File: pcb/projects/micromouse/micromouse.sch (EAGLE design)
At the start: 52 parts, among them M1 332-06, M2 332-06, U1 DSPIC33FJ64MC804-H/PTTQFP44_1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, U2 UA78M33CKCS, U3 UA78M05CKCS

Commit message: Replace some pin connectors
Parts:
- removed DIST1+, DIST1-, DIST1S, DIST2+, DIST2-, DIST2S, DIST3+, DIST3-, DIST3S, PAD+, PAD-: (no value), wirepad:SMD2
- removed M1, M2: 332-06, con-garry:332-06
- added DIST1, DIST2, DIST3: (no value), con-lstb:MA03-1
- added G1: AB9V, battery:AB9V
- added MOTOR1, MOTOR2: (no value), con-lstb:MA03-2
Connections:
- net +5V: now also DIST1.3, DIST2.3, DIST3.3; no longer DIST1+.P, DIST2+.P, DIST3+.P
- net DSENS1: now also DIST1.2; no longer DIST1S.P
- net DSENS2: now also DIST2.2; no longer DIST2S.P
- net DSENS3: now also DIST3.2; no longer DIST3S.P
- net GND: now also DIST1.1, DIST2.1, DIST3.1, G1.-, MOTOR1.3, MOTOR2.3; no longer DIST1-.P, DIST2-.P, DIST3-.P, M1-3.S, M2-3.S, PAD-.P
- net M1+: now also D2.C, D4.A, MOTOR1.2; no longer D3.C, D5.A, M1-6.S
- net M1-: now also D3.C, D5.A, MOTOR1.1; no longer D2.C, D4.A, M1-5.S
- net M1_EA: now also MOTOR1.6; no longer M1-2.S
- net M1_EB: now also MOTOR1.5; no longer M1-1.S
- net M2+: now also MOTOR2.2; no longer M2-6.S
- net M2-: now also MOTOR2.1; no longer M2-5.S
- net M2_EA: now also MOTOR2.6; no longer M2-2.S
- net M2_EB: now also MOTOR2.5; no longer M2-1.S
- net PAD+: now also G1.+; no longer PAD+.P
- net VDD: now also MOTOR1.4, MOTOR2.4; no longer M1-4.S, M2-4.S
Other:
- note added: "TODO: - Double-check pin connections for programmer and UART connector - Check connection for buttons"
- note removed: "TODO: - Decoupling capacitor for sensors? - Package for: - Diodes - Crystal - Buttons - Voltage Regulators"
- moved on the sheet: D6, D7, D8, D9

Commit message: Routing for new PCB
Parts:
- C8: value (none) -> 100nF
- R1: value 47k -> 10k
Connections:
- net N$1 renamed VCAP
- net PAD+ renamed +9V
- removed net N$6: PROG.6, R1.1, RESET.P, U1.!MCLR
- removed net N$8: PROG.3, U1.PGED1/AN2/C2IN-/RP0/CN4/RB0
- removed net N$9: PROG.2, U1.PGEC1/AN3/C2IN+/RP1/CN5/RB1
- new net ICSP_CLOCK: PROG.5, U1.PGEC1/AN3/C2IN+/RP1/CN5/RB1
- new net ICSP_DATA: PROG.4, U1.PGED1/AN2/C2IN-/RP0/CN4/RB0
- new net MCLR: PROG.1, R1.1, RESET.S, U1.!MCLR
- net DSENS1: now also U1.AN6/DAC1RM/RP16/CN8/RC0; no longer U1.AN4/C1IN-/RP2/CN6/RB2
- net DSENS2: now also U1.AN5/C1IN+/RP3/CN7/RB3; no longer U1.AN6/DAC1RM/RP16/CN8/RC0
- net DSENS3: now also U1.AN4/C1IN-/RP2/CN6/RB2; no longer U1.AN5/C1IN+/RP3/CN7/RB3
- net GND: now also PROG.3, UART.2; no longer PROG.4, UART.1
- net M1+: now also L293B1.OUTPUT4; no longer L293B1.OUTPUT1
- net M1-: now also L293B1.OUTPUT3; no longer L293B1.OUTPUT2
- net M1_D1: now also L293B1.INPUT3, U1.RP21/CN26/PMA3/RC5; no longer L293B1.INPUT1, U1.RP20/CN25/PMA4/RC4
- net M1_D2: now also L293B1.INPUT4, U1.RP20/CN25/PMA4/RC4; no longer L293B1.INPUT2, U1.RP21/CN26/PMA3/RC5
- net M1_EA: now also U1.TDI/PMA9/RA9; no longer U1.RP19/CN28/PMBE/RC3
- net M1_EB: now also U1.RP19/CN28/PMBE/RC3; no longer U1.TDI/PMA9/RA9
- net M1_PWM: now also L293B1.ENABLE2; no longer L293B1.ENABLE1
- net M2+: now also L293B1.OUTPUT2; no longer L293B1.OUTPUT3
- net M2-: now also L293B1.OUTPUT1; no longer L293B1.OUTPUT4
- net M2_D1: now also L293B1.INPUT1, U1.SDA1/RP9/CN21/PMD3/RB9; no longer L293B1.INPUT3, U1.PWM2H1/RP22/CN18/PMA1/RC6
- net M2_D2: now also L293B1.INPUT2, U1.PWM2H1/RP22/CN18/PMA1/RC6; no longer L293B1.INPUT4, U1.SDA1/RP9/CN21/PMD3/RB9
- net M2_EA: now also U1.PWM2L1/RP23/CN17/PMA0/RC7; no longer U1.RP24/CN20/PMA5/RC8
- net M2_EB: now also U1.RP24/CN20/PMA5/RC8; no longer U1.PWM2L1/RP23/CN17/PMA0/RC7
- net M2_PWM: now also L293B1.ENABLE1; no longer L293B1.ENABLE2
- net N$3: now also RESET.P; no longer RESET.P1
- net RX: now also UART.4; no longer UART.2
- net VDD: now also PROG.2, S1.S1, UART.1; no longer PROG.5, S1.P, UART.4
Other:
- note added: "TODO: - Double-check pin connections for programmer and UART connector - Add holes for LED on front"
- note removed: "TODO: - Double-check pin connections for programmer and UART connector - Check connection for buttons"
- moved on the sheet: R2, RESET, S1

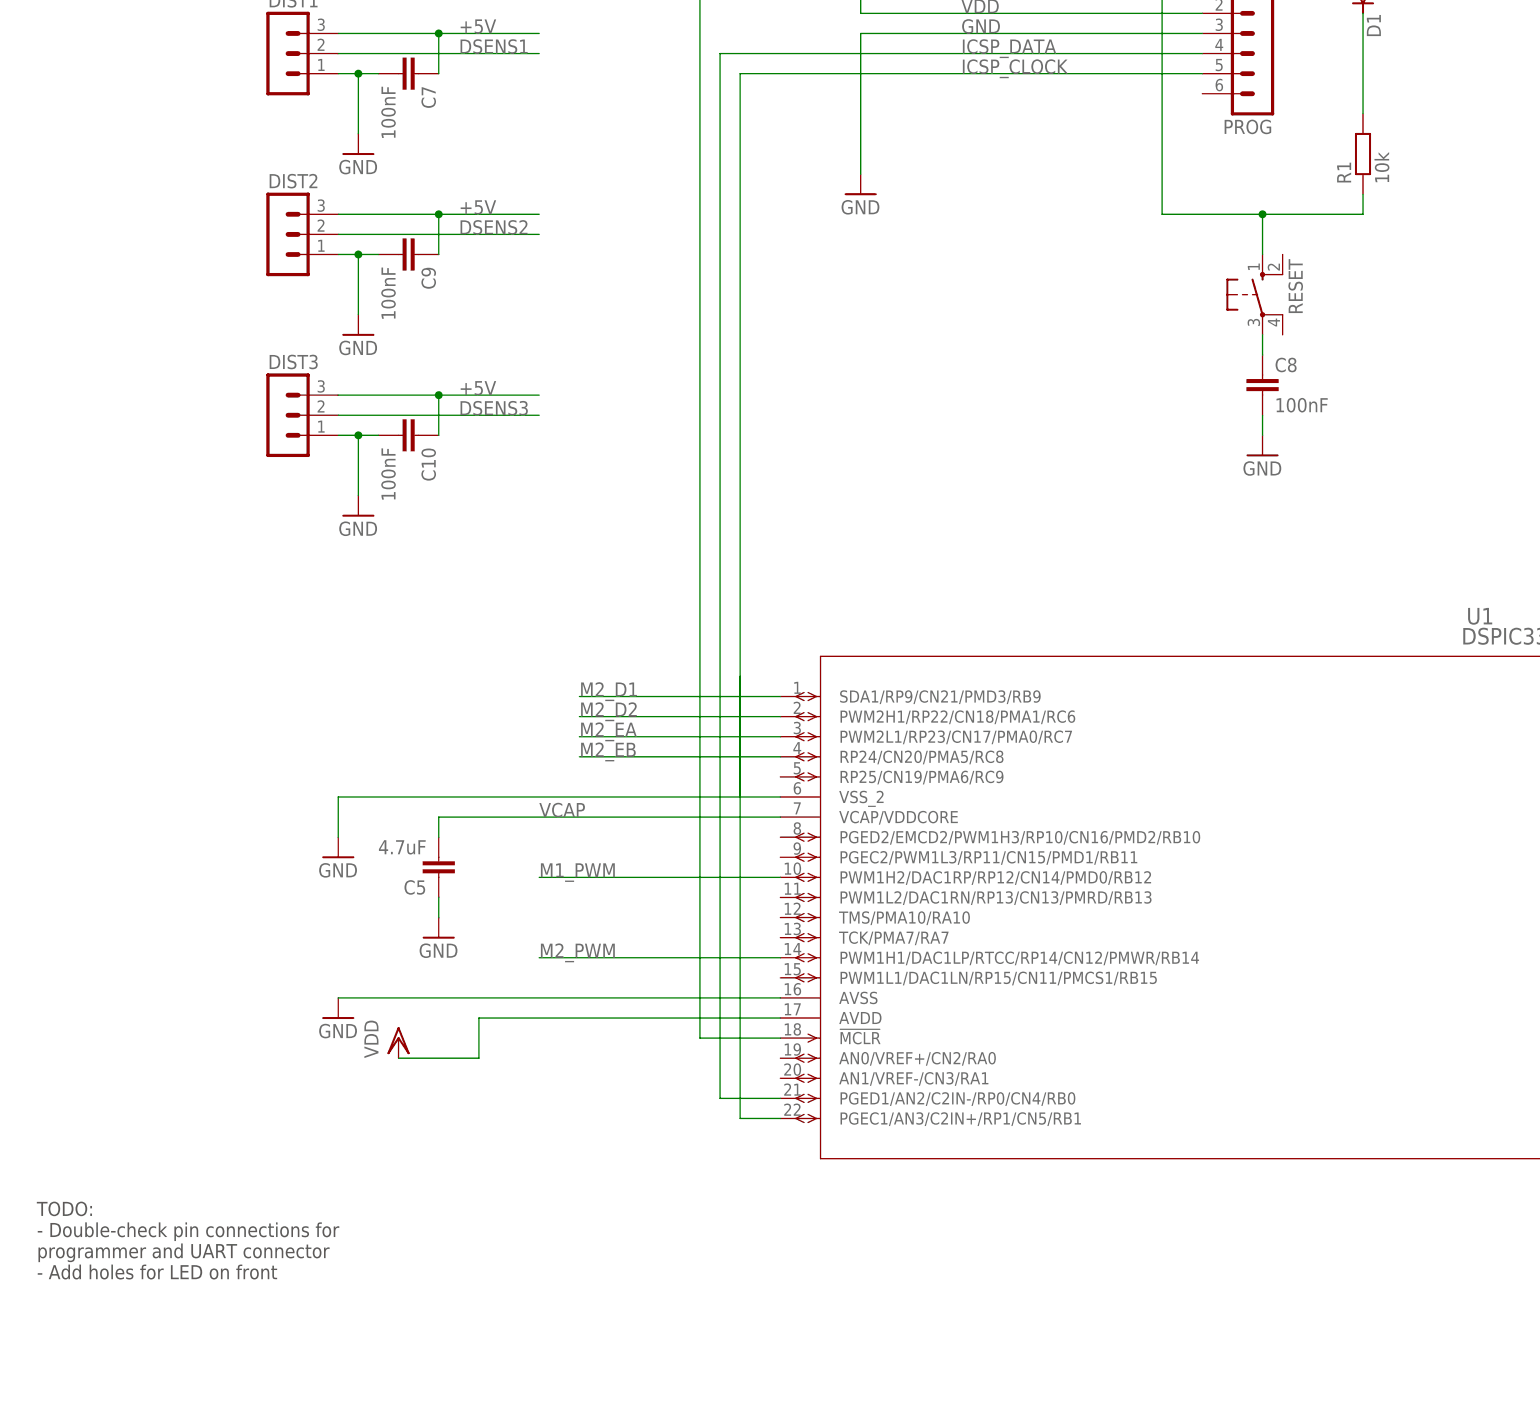
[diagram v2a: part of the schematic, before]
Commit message: Update reset button
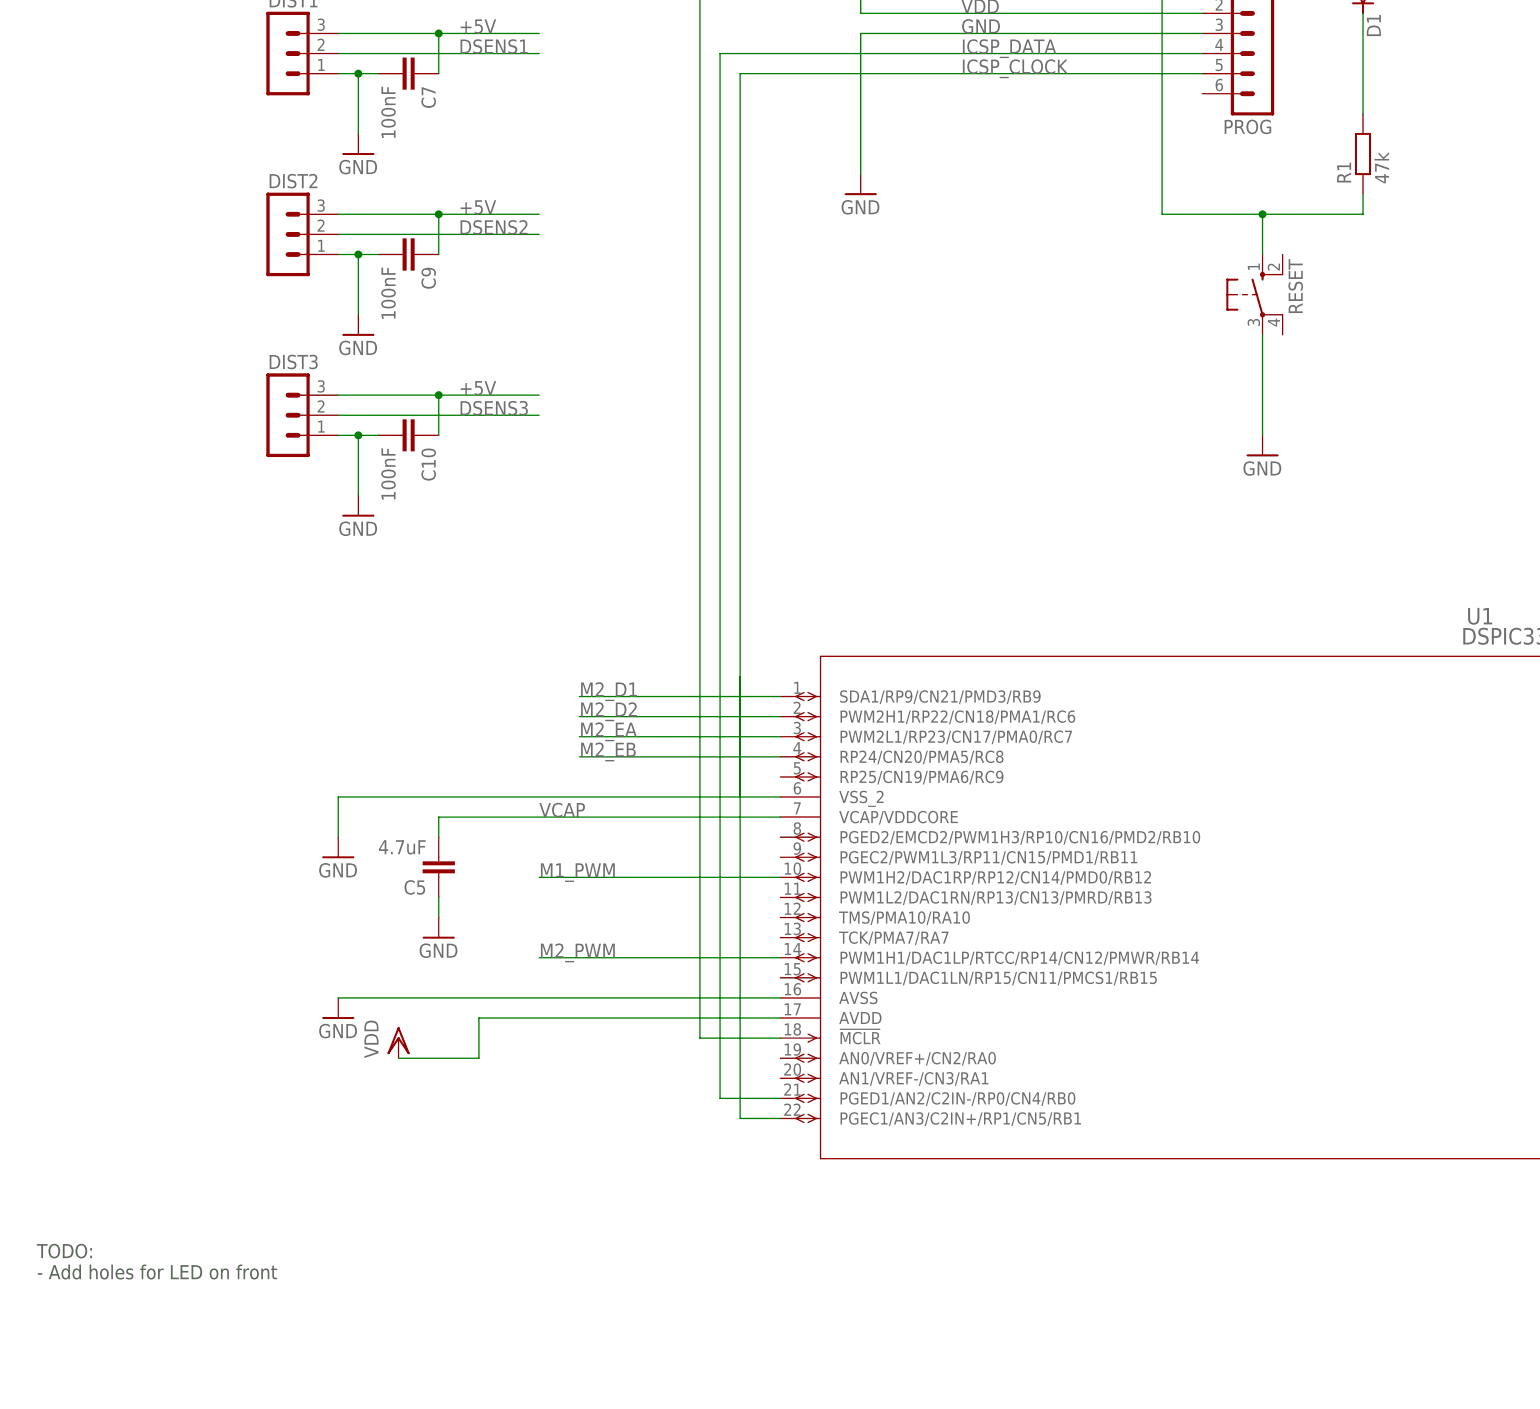
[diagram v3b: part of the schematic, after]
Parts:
- removed C8: 100nF, rcl:C-EUC0805
- R1: value 10k -> 47k
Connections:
- removed net N$3: C8.1, RESET.P
- net GND: now also RESET.P; no longer C8.2
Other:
- note added: "TODO: - Add holes for LED on front"
- note removed: "TODO: - Double-check pin connections for programmer and UART connector - Add holes for LED on front"
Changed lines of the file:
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@@
 <part name="VDD5" library="supply1" library_urn="urn:adsk.eagle:library:371" deviceset="VDD" device=""/>
 <part name="GND6" library="supply1" library_urn="urn:adsk.eagle:library:371" deviceset="GND" device=""/>
-<part name="R1" library="rcl" library_urn="urn:adsk.eagle:library:334" deviceset="R-EU_" device="R0805" package3d_urn="urn:adsk.eagle:package:23553/2" value="10k"/>
+<part name="R1" library="rcl" library_urn="urn:adsk.eagle:library:334" deviceset="R-EU_" device="R0805" package3d_urn="urn:adsk.eagle:package:23553/2" value="47k"/>
 <part name="D1" library="diode" library_urn="urn:adsk.eagle:library:210" deviceset="DIODE-" device="SOD123" package3d_urn="urn:adsk.eagle:package:43420/1"/>
 <part name="VDD6" library="supply1" library_urn="urn:adsk.eagle:library:371" deviceset="VDD" device=""/>
@@
 <part name="GND13" library="supply1" library_urn="urn:adsk.eagle:library:371" deviceset="GND" device=""/>
 <part name="VDD11" library="supply1" library_urn="urn:adsk.eagle:library:371" deviceset="VDD" device=""/>
-<part name="C8" library="rcl" library_urn="urn:adsk.eagle:library:334" deviceset="C-EU" device="C0805" package3d_urn="urn:adsk.eagle:package:23617/2" value="100nF"/>
 <part name="GND15" library="supply1" library_urn="urn:adsk.eagle:library:371" deviceset="GND" device=""/>
 <part name="VDD12" library="supply1" library_urn="urn:adsk.eagle:library:371" deviceset="VDD" device=""/>
@@
 <text x="251.46" y="66.04" size="1.778" layer="93">Motor 2</text>
 <text x="22.86" y="86.36" size="1.778" layer="97">TODO:
-- Double-check pin connections for
-programmer and UART connector
 - Add holes for LED on front</text>
 <text x="386.08" y="129.54" size="1.778" layer="93">Oscillator</text>
@@
 <attribute name="VALUE" x="340.36" y="149.86" size="1.778" layer="96" rot="R90"/>
 </instance>
-<instance part="C8" gate="G$1" x="177.8" y="200.66" smashed="yes">
-<attribute name="NAME" x="179.324" y="201.041" size="1.778" layer="95"/>
-<attribute name="VALUE" x="179.324" y="195.961" size="1.778" layer="96"/>
-</instance>
 <instance part="GND15" gate="1" x="60.96" y="119.38" smashed="yes">
 <attribute name="VALUE" x="58.42" y="116.84" size="1.778" layer="96"/>
@@
 </segment>
 <segment>
-<pinref part="C8" gate="G$1" pin="2"/>
 <pinref part="GND8" gate="1" pin="GND"/>
-<wire x1="177.8" y1="195.58" x2="177.8" y2="193.04" width="0.1524" layer="91"/>
+<pinref part="RESET" gate="1" pin="P"/>
+<wire x1="177.8" y1="205.74" x2="177.8" y2="193.04" width="0.1524" layer="91"/>
 </segment>
 <segment>
@@
 </segment>
 </net>
-<net name="N$3" class="0">
-<segment>
-<pinref part="RESET" gate="1" pin="P"/>
-<pinref part="C8" gate="G$1" pin="1"/>
-<wire x1="177.8" y1="205.74" x2="177.8" y2="203.2" width="0.1524" layer="91"/>
-</segment>
-</net>

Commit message: LED and resistor value
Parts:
- added LED3: (no value), led:LED3MM
- R2: value (none) -> 10k
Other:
- note added: "This LED is solely for keeping the front off the ground."
- note removed: "TODO: - Add holes for LED on front"
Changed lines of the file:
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@@
 <part name="VDD3" library="supply1" library_urn="urn:adsk.eagle:library:371" deviceset="VDD" device=""/>
 <part name="GND19" library="supply1" library_urn="urn:adsk.eagle:library:371" deviceset="GND" device=""/>
-<part name="R2" library="rcl" library_urn="urn:adsk.eagle:library:334" deviceset="R-EU_" device="R0805" package3d_urn="urn:adsk.eagle:package:23553/2"/>
+<part name="R2" library="rcl" library_urn="urn:adsk.eagle:library:334" deviceset="R-EU_" device="R0805" package3d_urn="urn:adsk.eagle:package:23553/2" value="10k"/>
 <part name="LED1" library="led" library_urn="urn:adsk.eagle:library:259" deviceset="LED" device="CHIP-LED0805" package3d_urn="urn:adsk.eagle:package:15818/2"/>
 <part name="LED2" library="led" library_urn="urn:adsk.eagle:library:259" deviceset="LED" device="CHIP-LED0805" package3d_urn="urn:adsk.eagle:package:15818/2"/>
@@
 <part name="DIST3" library="con-lstb" library_urn="urn:adsk.eagle:library:162" deviceset="MA03-1" device="" package3d_urn="urn:adsk.eagle:package:8339/1"/>
 <part name="G1" library="battery" library_urn="urn:adsk.eagle:library:109" deviceset="AB9V" device="" package3d_urn="urn:adsk.eagle:package:4600/1"/>
+<part name="LED3" library="led" library_urn="urn:adsk.eagle:library:259" deviceset="LED" device="3MM" package3d_urn="urn:adsk.eagle:package:15797/1"/>
 </parts>
 <sheets>
@@
 <text x="35.56" y="60.96" size="1.778" layer="93">Motor 1</text>
 <text x="251.46" y="66.04" size="1.778" layer="93">Motor 2</text>
-<text x="22.86" y="86.36" size="1.778" layer="97">TODO:
-- Add holes for LED on front</text>
 <text x="386.08" y="129.54" size="1.778" layer="93">Oscillator</text>
 <text x="365.76" y="259.08" size="1.778" layer="97">These capacitors are the decoupling capacitors for the
@@
 datasheet section 2.2</text>
 <text x="358.14" y="58.42" size="1.778" layer="97">Button und LEDs</text>
+<text x="391.16" y="50.8" size="1.778" layer="96">This LED is solely for keeping
+the front off the ground.</text>
 </plain>
 <instances>
@@
 <attribute name="VALUE" x="223.52" y="230.505" size="1.778" layer="96" rot="R90"/>
 </instance>
+<instance part="LED3" gate="G$1" x="386.08" y="48.26" smashed="yes">
+<attribute name="NAME" x="389.636" y="43.688" size="1.778" layer="95" rot="R90"/>
+<attribute name="VALUE" x="391.795" y="43.688" size="1.778" layer="96" rot="R90"/>
+</instance>
 </instances>

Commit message: Update
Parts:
- removed LED3: (no value), led:LED3MM
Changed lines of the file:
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@@
 <part name="DIST3" library="con-lstb" library_urn="urn:adsk.eagle:library:162" deviceset="MA03-1" device="" package3d_urn="urn:adsk.eagle:package:8339/1"/>
 <part name="G1" library="battery" library_urn="urn:adsk.eagle:library:109" deviceset="AB9V" device="" package3d_urn="urn:adsk.eagle:package:4600/1"/>
-<part name="LED3" library="led" library_urn="urn:adsk.eagle:library:259" deviceset="LED" device="3MM" package3d_urn="urn:adsk.eagle:package:15797/1"/>
 </parts>
 <sheets>
@@
 <attribute name="VALUE" x="223.52" y="230.505" size="1.778" layer="96" rot="R90"/>
 </instance>
-<instance part="LED3" gate="G$1" x="386.08" y="48.26" smashed="yes">
-<attribute name="NAME" x="389.636" y="43.688" size="1.778" layer="95" rot="R90"/>
-<attribute name="VALUE" x="391.795" y="43.688" size="1.778" layer="96" rot="R90"/>
-</instance>
 </instances>
